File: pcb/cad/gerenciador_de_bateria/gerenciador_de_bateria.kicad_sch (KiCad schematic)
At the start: 83 parts, among them J1 Conn_01x02_Male, J10 Conn_01x02_Male, J11 Conn_01x02_Male, J12 Conn_01x02_Male, J13 Conn_01x02_Male, J14 Conn_01x03_Male, J15 Conn_02x02_Odd_Even, J16 Conn_01x02_Male, J17 Conn_01x02_Male, J18 Conn_01x02_Male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

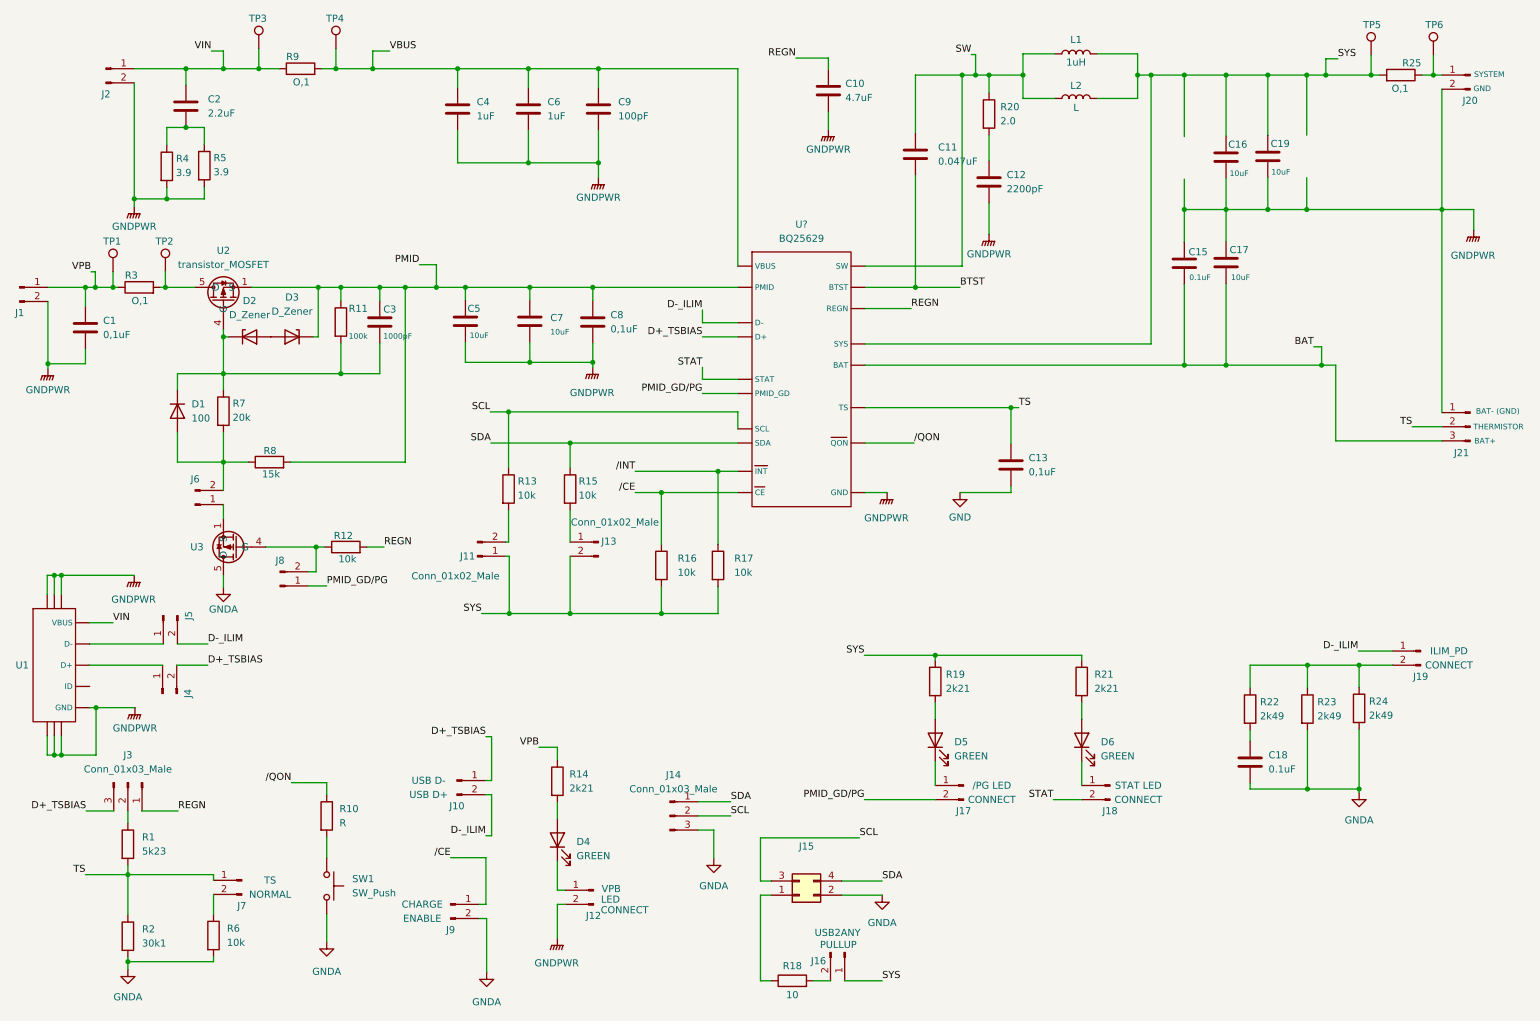
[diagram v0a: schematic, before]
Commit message: Atualização dos esquemáticos de PCB para gerenciadores de bateria
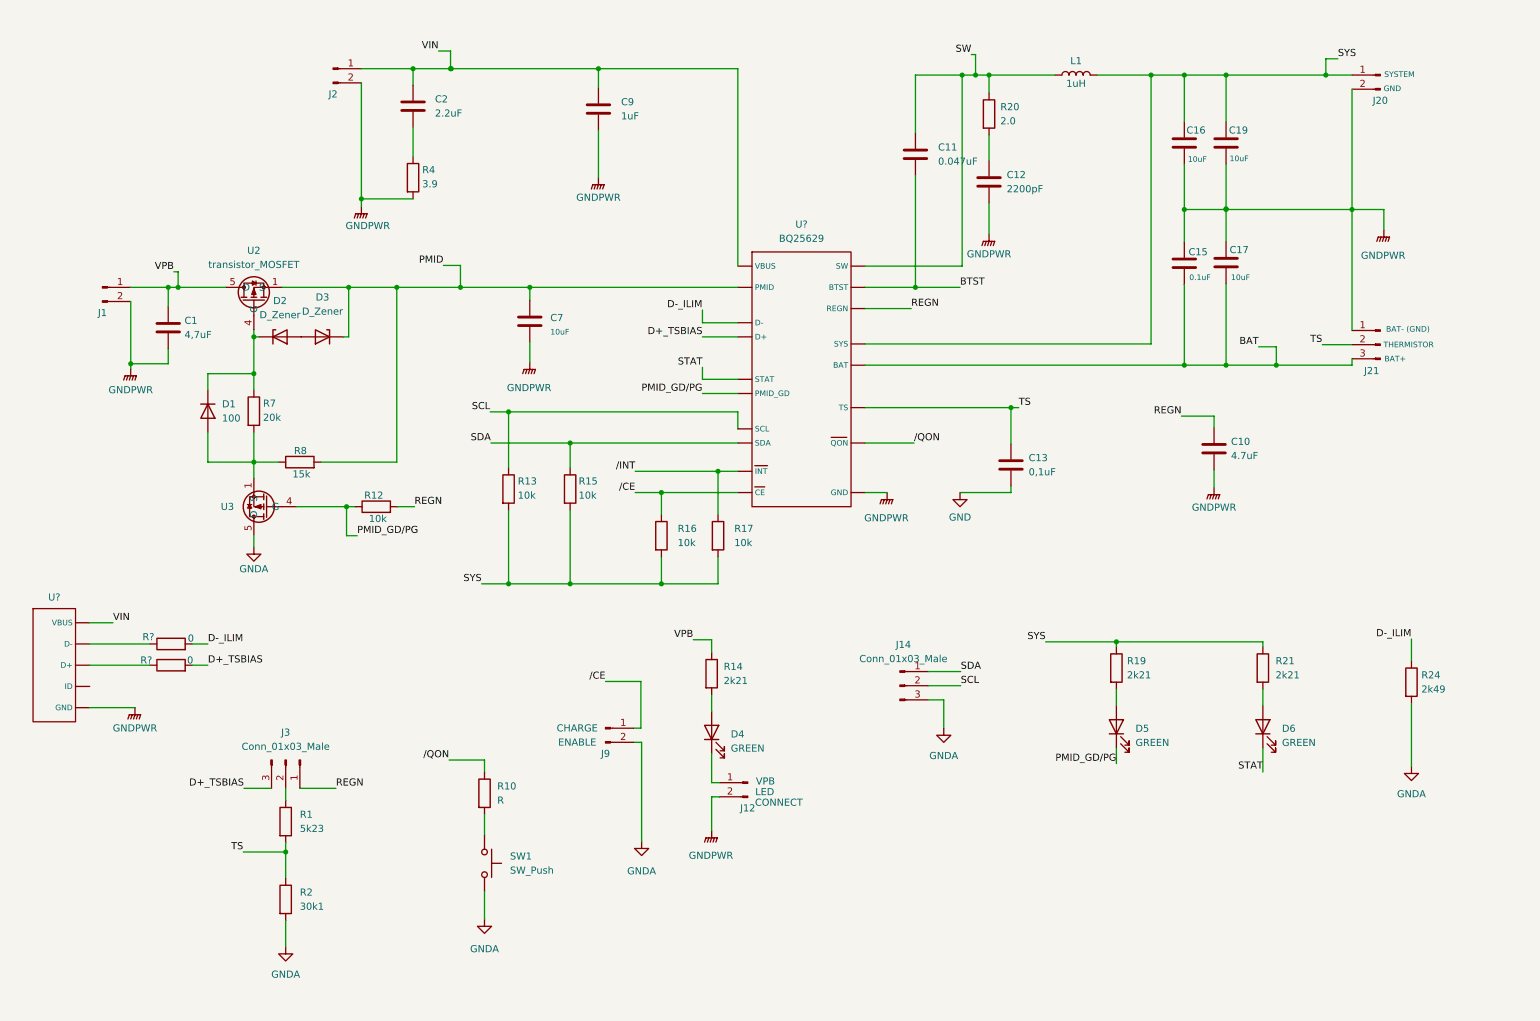
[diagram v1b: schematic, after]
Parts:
- removed C18: 0.1uF, symbol Device:C
- removed C3: 1000pF, symbol Device:C
- removed C4, C6: 1uF, symbol Device:C
- removed C5: 10uF, symbol Device:C
- removed C8: 0,1uF, symbol Device:C
- removed J10, J11, J13, J16, J17, J18, J19, J4, J5, J6, J7, J8: Conn_01x02_Male, symbol Connector:Conn_01x02_Male
- removed J15: Conn_02x02_Odd_Even, symbol Connector_Generic:Conn_02x02_Odd_Even
- removed L2: L, symbol Device:L
- removed R11: 100k, symbol Device:R
- removed R18: 10, symbol Device:R
- removed R22, R23: 2k49, symbol Device:R
- removed R25, R3, R9: O,1, symbol Device:R
- removed R5: 3.9, symbol Device:R
- removed R6: 10k, symbol Device:R
- removed TP1, TP2, TP3, TP4, TP5, TP6: TestPoint, symbol Connector:TestPoint
- removed U1: USB_BQ25629, symbol gerenciador_de_bateria_simbolos:USB_BQ25629
- added R? (x2): 0, symbol Device:R
- added U?: USB_BQ25629, symbol gerenciador_de_bateria_simbolos:USB_BQ25629
- C1: value 0,1uF -> 4,7uF
- C9: value 100pF -> 1uF
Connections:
- net D+_TSBIAS: now also R?.2
- net D-_ILIM: now also R24.1, R?.2
- net GNDPWR: now also U?. (VBUS)
- net PMID_GD/PG: now also D5.1 (K), R12.1, U3.4 (G)
- net STAT: now also D6.1 (K)
- net SYS: now also J20.1 (Pin_1), R13.2, R15.2
- net VIN: now also C9.1, U?. (VBUS), U?. (VBUS)
- net VPB: now also U2.5 (D)
- net at U3.1 (S), U3.2 (S), U3.3 (S): now also D1.2 (A), R7.2, R8.1
- removed net VBUS: C9.1, U?. (VBUS)
- new net: R?.1, U?. (VBUS) (x2)
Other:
- moved on the sheet: C1, C10, C16, C19, C2, D1, D2, D3, D4, D5, D6, J1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

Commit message: Atualização dos esquemáticos dos gerenciadores de bateria
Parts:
- added R6: 0, symbol Device:R
- D1: value 100 -> 100V
- R10: value R -> 4k7
- gave numbers to parts that had none: 4
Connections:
- net GND: now also R6.2
- net GNDPWR: now also R6.1
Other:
- moved on the sheet: C12, R20

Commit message: Associação dos footprint e início do layout da PCB
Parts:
- C1, C10, C11, C12, C13, C15, C16, C17, C19, C2, C7, C9: footprint (none) -> Capacitor_SMD:C_0805_2012Metric
- D1, D2, D3: footprint (none) -> Diode_SMD:D_0805_2012Metric
- D4, D5, D6: footprint (none) -> LED_SMD:LED_0805_2012Metric
- J1, J12, J2, J20, J9: footprint (none) -> Connector_PinHeader_2.54mm:PinHeader_1x02_P2.54mm_Vertical
- J14, J21, J3: footprint (none) -> Connector_PinHeader_2.54mm:PinHeader_1x03_P2.54mm_Vertical
- L1: footprint (none) -> Inductor_SMD:L_0805_2012Metric
- R1, R10, R12, R13, R14, R15, R16, R17, R19, R2, R20, R21, R24, R3, R4, R5, R6, R7, R8: footprint (none) -> Resistor_SMD:R_0805_2012Metric
- SW1: footprint (none) -> Button_Switch_THT:SW_PUSH_6mm
- U1: footprint (none) -> Connector_USB:USB_Micro-B_Amphenol_10118194_Horizontal
- U4: footprint (none) -> gerenciador_de_bateria_fp:WQFN-HR18_RYK_TEX

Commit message: Associação de footprints e inicio do layout de pCB.
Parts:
- removed D1: 100V, Diode_SMD:D_0805_2012Metric, symbol Device:D
- removed D2, D3: D_Zener, Diode_SMD:D_0805_2012Metric, symbol Device:D_Zener
- removed U2, U3: transistor_MOSFET, symbol gerenciador_de_bateria_simbolos:transistor_MOSFET
- added Q1: ZVN4106F, Package_TO_SOT_SMD:SOT-23, symbol Transistor_FET:ZVN4106F
- added Q2: BC817, Package_TO_SOT_SMD:SOT-23, symbol Transistor_BJT:BC817
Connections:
- net BAT: now also U4.8 (BAT); no longer U4. (VBUS)
- net BTST: now also U4.1 (BTST); no longer U4. (VBUS)
- net D+_TSBIAS: now also U4.5 (D+); no longer U4. (VBUS)
- net D-_ILIM: now also U4.4 (D-); no longer U4. (VBUS)
- net GNDA: now also Q1.3 (D)
- net GNDPWR: now also U4.15 (GND); no longer U4. (VBUS)
- net PMID: now also U4.17 (PMID), Q2.2 (E); no longer U4. (VBUS)
- net PMID_GD/PG: now also U4.3 (PMID_GD), Q1.1 (G); no longer U4. (VBUS)
- net REGN: now also U4.2 (REGN); no longer U4. (VBUS)
- net SCL: now also U4.13 (SCL); no longer U4. (VBUS)
- net SDA: now also U4.12 (SDA); no longer U4. (VBUS)
- net STAT: now also U4.10 (STAT); no longer U4. (VBUS)
- net SW: now also U4.16 (SW); no longer U4. (VBUS)
- net SYS: now also U4.9 (SYS); no longer U4. (VBUS)
- net TS: now also U4.6 (TS); no longer U4. (VBUS)
- net VIN: now also U4.18 (VBUS); no longer U4. (VBUS)
- net VPB: now also Q2.3 (C)
- net /CE: now also U4.14 (CE); no longer U4. (VBUS)
- net /INT: now also U4.11 (INT); no longer U4. (VBUS)
- net /QON: now also U4.7 (QON); no longer U4. (VBUS)
- net at R7.1: now also Q2.1 (B)
- net at R7.2, R8.1: now also Q1.2 (S)
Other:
- moved on the sheet: R7, R8

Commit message: Inicio do layout de PCB
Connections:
- net GNDPWR: now also U1.5 (GND); no longer U1. (VBUS)
- net VIN: now also U1.1 (VBUS); no longer U1. (VBUS)
- net at R5.1: now also U1.3 (D+); no longer U1. (VBUS)
- net at R3.1: now also U1.2 (D-); no longer U1. (VBUS)
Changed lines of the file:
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@@
     (pin "2")
+  )
+  (symbol (lib_id "gerenciador_de_bateria_simbolos:USB_BQ25629") (at 20.193 122.682 0) (unit 1)
+    (in_bom yes) (on_board yes) (fields_autoplaced)
+    (property "Reference" "U1" (id 0) (at 20.193 123.19 0))
+    (property "Value" "USB_BQ25629" (id 1) (at 18.923 122.682 0)
+      (effects (font (size 1.27 1.27)) hide)
+    )
+    (property "Footprint" "Connector_USB:USB_Micro-B_Amphenol_10118194_Horizontal" (id 2) (at 18.923 122.682 0)
+      (effects (font (size 1.27 1.27)) hide)
+    )
+    (property "Datasheet" "" (id 3) (at 18.923 122.682 0)
+      (effects (font (size 1.27 1.27)) hide)
+    )
+    (pin "1")
+    (pin "2")
+    (pin "3")
+    (pin "4")
+    (pin "5")
   )
   (symbol (lib_id "power:GNDA") (at 263.779 153.543 0) (unit 1)
@@
     (pin "1")
     (pin "2")
-  )
-  (symbol (lib_id "gerenciador_de_bateria_simbolos:USB_BQ25629") (at 20.193 122.682 0) (unit 1)
-    (in_bom yes) (on_board yes) (fields_autoplaced)
-    (property "Reference" "U1" (id 0) (at 20.193 123.19 0))
-    (property "Value" "USB_BQ25629" (id 1) (at 18.923 122.682 0)
-      (effects (font (size 1.27 1.27)) hide)
-    )
-    (property "Footprint" "Connector_USB:USB_Micro-B_Amphenol_10118194_Horizontal" (id 2) (at 18.923 122.682 0)
-      (effects (font (size 1.27 1.27)) hide)
-    )
-    (property "Datasheet" "" (id 3) (at 18.923 122.682 0)
-      (effects (font (size 1.27 1.27)) hide)
-    )
-    (pin "")
-    (pin "")
-    (pin "")
-    (pin "")
-    (pin "")
   )
   (symbol (lib_id "Connector:Conn_01x02_Male") (at 119.126 146.685 0) (unit 1)
@@
       (reference "SW1") (unit 1) (value "SW_Push") (footprint "Button_Switch_THT:SW_PUSH_6mm")
     )
-    (path "/5a500ca0-5070-4070-9db4-317eceeb18a4"
+    (path "/1735d2a5-2985-4656-a97e-5f0f85724d56"
       (reference "U1") (unit 1) (value "USB_BQ25629") (footprint "Connector_USB:USB_Micro-B_Amphenol_10118194_Horizontal")
     )
